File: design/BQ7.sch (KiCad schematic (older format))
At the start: 43 parts

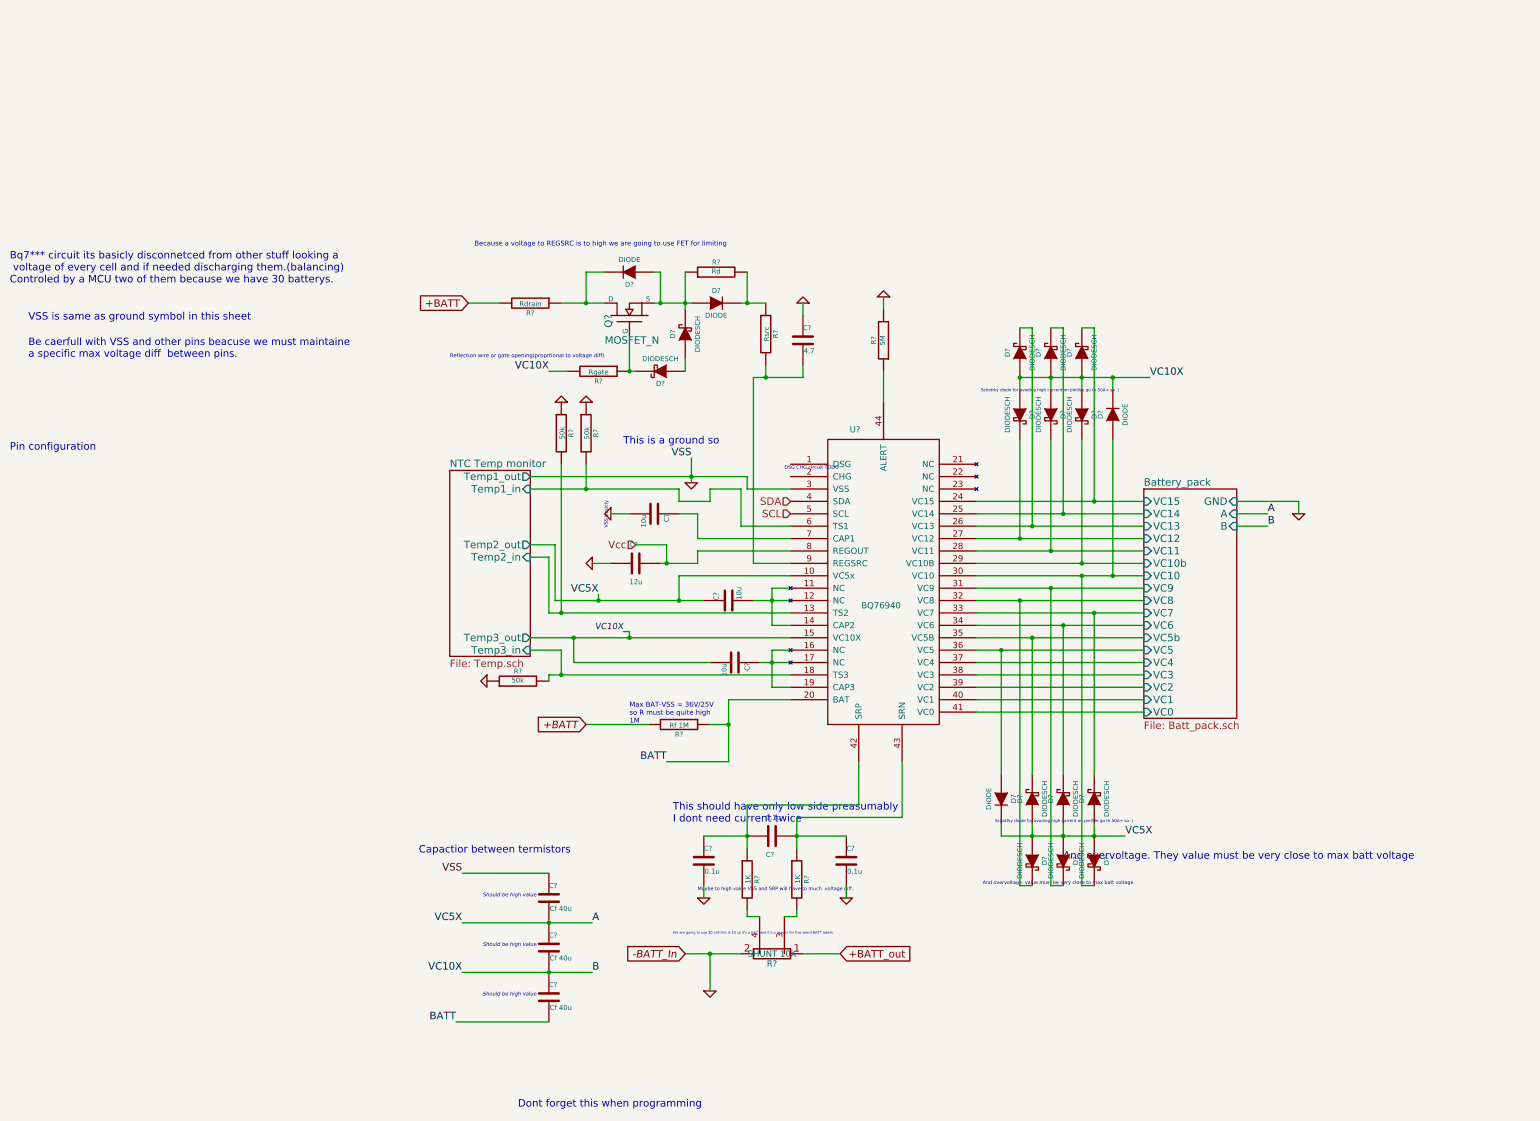
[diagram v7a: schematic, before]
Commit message: Add new example in datasheet define more values
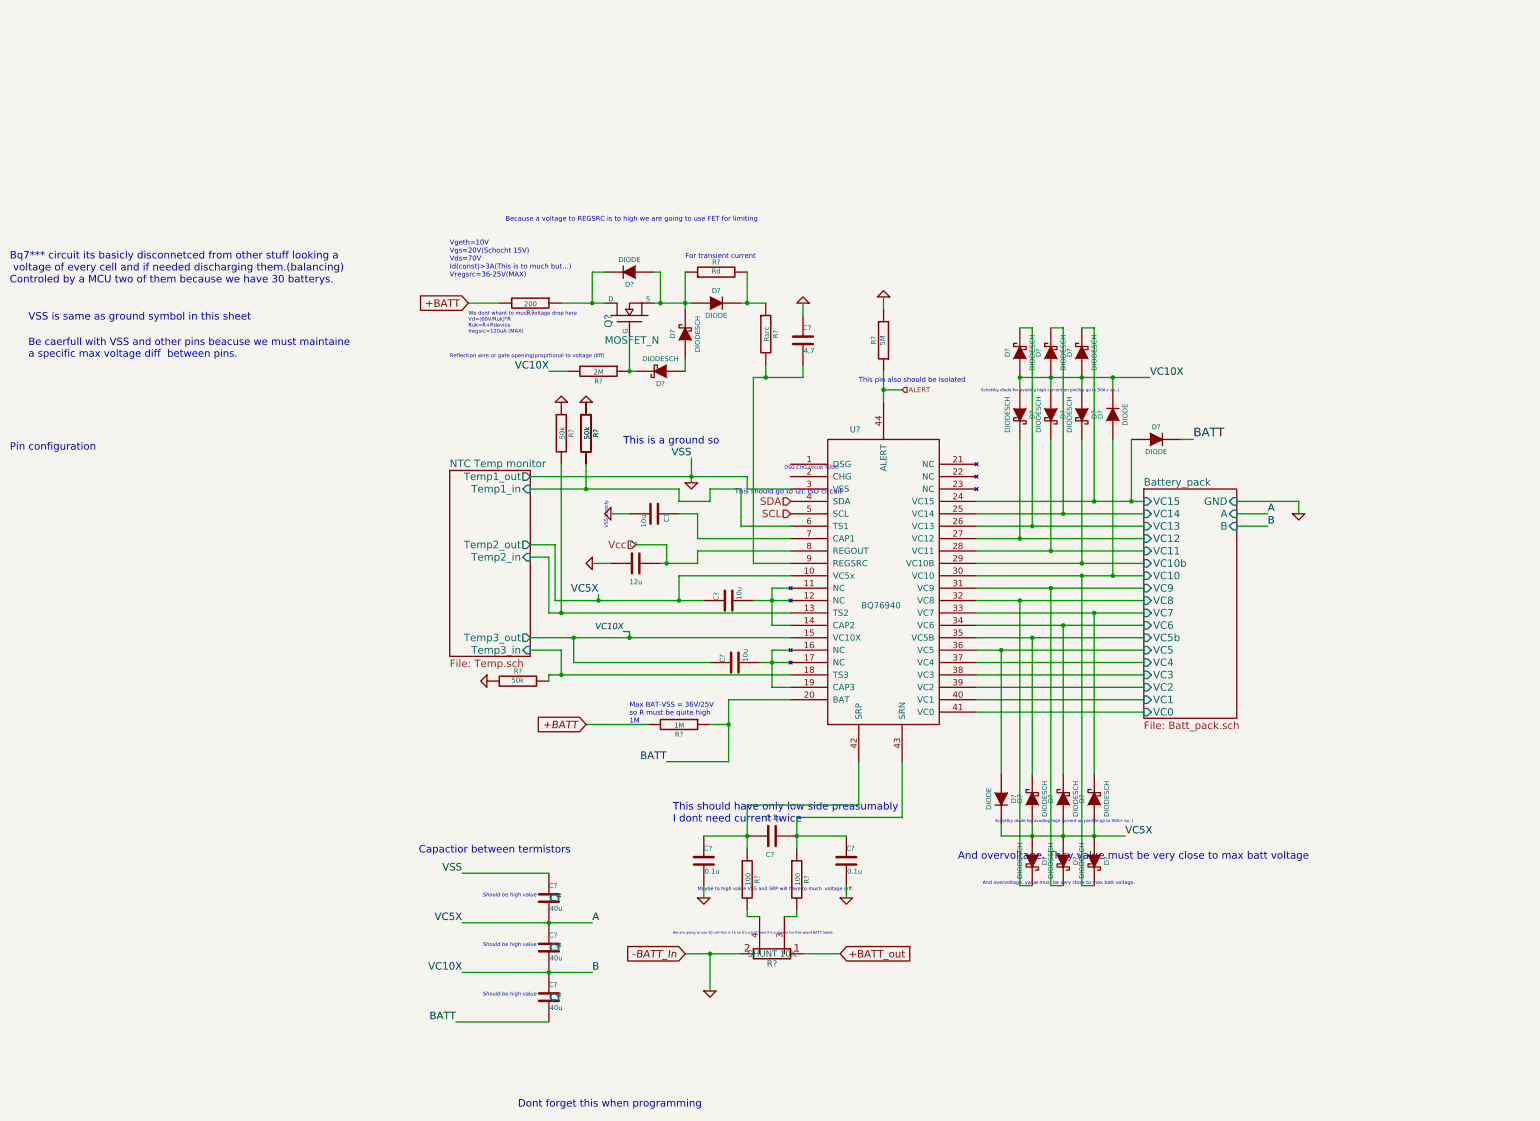
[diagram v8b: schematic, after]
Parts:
- removed C? (x2): Cf 40u, symbol C
- added C? (x2): 40u, symbol C
- added D?: DIODE, symbol DIODE
- added R?: 50k, symbol R
- C?: value Cf 40u -> 40u; Name (none) -> Cf
- R? (x2): value 1K -> 100
- R?: value Rgate -> 2M; Name (none) -> Rgate
- R?: value Rdrain -> 200; Name (none) -> Rdrain
- R?: value Rf 1M -> 1M; Name (none) -> Rf
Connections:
- net A: now also C?.1, C?.2
- net B: now also C?.1, C?.2; no longer C?.2
- net BATT: now also D?.2 (K)
- net Battery_pack/VC15: now also D?.1 (A)
- net GND: now also C?.1, R?.1
- net NTC Temp monitor/Temp1_in: now also R?.2
- net ALERT: now reaches R?.1, U?.44 (ALERT)
- net at U?.16 (NC), U?.17 (NC), U?.19 (CAP3): now also C?.2; no longer C?.1
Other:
- note added: "For transient current"
- note added: "This pin also should be isolated"
- note added: "This should go to i2c ISO circuit"
- note added: "Vgeth=10V\nVgs=20V(Schocht 15V)\nVds=70V\nId(const)>3A(This is to much but...)\nVregsrc=36-25V(MAX)"
- note added: "We dont whant to much voltage drop here\nVd=(60V/Ruk)*R\nRuk=R+Rdevice\nIregsrc=120uA (MAX)\n \n"
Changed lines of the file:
@@
 9F DF D1 D1 31 D6 A5 40 90 E1 4D 94 96 C0 77 F7 E1 9C E9 BB 40 B5 84 6A 00 41 90 F1 06 B5 8D 23
 08 82 20 C8 04 83 62 36 82 20 08 82 4C 0C 38 D4 12 88 20 08 82 20 E3 1C 1A 1D 89 20 08 82 20 08
-82 20 08 82 20 23 ED FF 01 11 4E 07 64 6B 3C CF 2D 00 00 00 00 49 45 4E 44 AE 42 60 82 A6
+82 20 08 82 20 23 ED FF 01 11 4E 07 64 6B 3C CF 2D 00 00 00 00 49 45 4E 44 AE 42 60 82 6A
 EndData
 $EndBitmap
@@
 P 6600 5650
 F 0 "R?" V 6680 5650 40  0000 C CNN
-F 1 "1K" V 6607 5651 40  0000 C CNN
+F 1 "100" V 6607 5651 40  0000 C CNN
 F 2 "" V 6530 5650 30  0000 C CNN
 F 3 "" H 6600 5650 30  0000 C CNN
@@
 P 7000 5650
 F 0 "R?" V 7080 5650 40  0000 C CNN
-F 1 "1K" V 7007 5651 40  0000 C CNN
+F 1 "100" V 7007 5651 40  0000 C CNN
 F 2 "" V 6930 5650 30  0000 C CNN
 F 3 "" H 7000 5650 30  0000 C CNN
@@
 P 6050 4400
 F 0 "R?" V 6130 4400 40  0000 C CNN
-F 1 "Rf 1M" V 6057 4401 40  0000 C CNN
+F 1 "1M" V 6057 4401 40  0000 C CNN
 F 2 "" V 5980 4400 30  0000 C CNN
 F 3 "" H 6050 4400 30  0000 C CNN
+F 4 "Rf" V 6050 4400 60  0001 C CNN "Name"
 	1    6050 4400
 	0    1    1    0
@@
 P 5400 1550
 F 0 "R?" V 5480 1550 40  0000 C CNN
-F 1 "Rgate" V 5407 1551 40  0000 C CNN
+F 1 "2M" V 5407 1551 40  0000 C CNN
 F 2 "" V 5330 1550 30  0000 C CNN
 F 3 "" H 5400 1550 30  0000 C CNN
+F 4 "Rgate" V 5400 1550 60  0001 C CNN "Name"
 	1    5400 1550
 	0    1    1    0
@@
 P 4850 1000
 F 0 "R?" V 4930 1000 40  0000 C CNN
-F 1 "Rdrain" V 4857 1001 40  0000 C CNN
+F 1 "200" V 4857 1001 40  0000 C CNN
 F 2 "" V 4780 1000 30  0000 C CNN
 F 3 "" H 4850 1000 30  0000 C CNN
+F 4 "Rdrain" V 4850 1000 60  0001 C CNN "Name"
 	1    4850 1000
 	0    1    1    0
@@
 Text Label 4300 6000 2    60   ~ 0
 VC5X
-$Comp
-L C C?
-U 1 1 55BD7EDC
-P 5000 5800
-F 0 "C?" H 5000 5900 40  0000 L CNN
-F 1 "Cf 40u" H 5006 5715 40  0000 L CNN
-F 2 "" H 5038 5650 30  0000 C CNN
-F 3 "" H 5000 5800 60  0000 C CNN
-	1    5000 5800
-	1    0    0    -1
-$EndComp
-$Comp
-L C C?
-U 1 1 55BD7FD5
-P 5000 6200
-F 0 "C?" H 5000 6300 40  0000 L CNN
-F 1 "Cf 40u" H 5006 6115 40  0000 L CNN
-F 2 "" H 5038 6050 30  0000 C CNN
-F 3 "" H 5000 6200 60  0000 C CNN
-	1    5000 6200
-	1    0    0    -1
-$EndComp
 Text Label 5950 4700 2    60   ~ 0
 BATT
@@
 P 5000 6600
 F 0 "C?" H 5000 6700 40  0000 L CNN
-F 1 "Cf 40u" H 5006 6515 40  0000 L CNN
+F 1 "40u" H 5006 6515 40  0000 L CNN
 F 2 "" H 5038 6450 30  0000 C CNN
 F 3 "" H 5000 6600 60  0000 C CNN
+F 4 "Cf" H 5001 6600 60  0000 L CNB "Name"
 	1    5000 6600
 	1    0    0    -1
@@
 Text Notes 4900 6600 2    30   Italic 0
 Should be high value\n
-Text Notes 4400 550  0    39   ~ 0
+Text Notes 4650 350  0    39   ~ 0
 Because a voltage to REGSRC is to high we are going to use FET for limiting
 Text Notes 4200 1450 0    31   ~ 0
@@
 Text Notes 6000 6100 0    20   ~ 0
 We are going to use 30 cell this is 15 so it's a half here it's a reason for this wierd BATT labels
-Text Notes 9150 5500 0    60   ~ 0
+Text Notes 8300 5500 0    60   ~ 0
 And overvoltage. They value must be very close to max batt voltage
 Text Notes 8500 5700 0    28   ~ 0
@@
 F 3 "" H 6500 3900 60  0000 C CNN
 	1    6500 3900
-	0    1    1    0
+	0    -1   -1   0
 $EndComp
 $Comp
@@
 Text Notes 6000 5200 0    60   ~ 0
 This should have only low side preasumably\nI dont need current twice
+Text Notes 6500 2550 0    40   ~ 0
+This should go to i2c ISO circuit
+$Comp
+L R R?
+U 1 1 55DBFB03
+P 5300 2050
+F 0 "R?" V 5380 2050 40  0000 C CNN
+F 1 "50k" V 5307 2051 40  0000 C CNN
+F 2 "" V 5230 2050 30  0000 C CNN
+F 3 "" H 5300 2050 30  0000 C CNN
+	1    5300 2050
+	1    0    0    -1
+$EndComp
+$Comp
+L C C?
+U 1 1 55DC3CEE
+P 5000 6200
+F 0 "C?" H 5000 6300 40  0000 L CNN
+F 1 "40u" H 5006 6115 40  0000 L CNN
+F 2 "" H 5038 6050 30  0000 C CNN
+F 3 "" H 5000 6200 60  0000 C CNN
+F 4 "Cf" H 5001 6200 60  0000 L CNB "Name"
+	1    5000 6200
+	1    0    0    -1
+$EndComp
+$Comp
+L C C?
+U 1 1 55DC3FA9
+P 5000 5800
+F 0 "C?" H 5000 5900 40  0000 L CNN
+F 1 "40u" H 5006 5715 40  0000 L CNN
+F 2 "" H 5038 5650 30  0000 C CNN
+F 3 "" H 5000 5800 60  0000 C CNN
+F 4 "Cf" H 5001 5800 60  0000 L CNB "Name"
+	1    5000 5800
+	1    0    0    -1
+$EndComp
+Text HLabel 7850 1700 2    40   Input ~ 0
+ALERT
+Text Notes 7500 1650 0    40   ~ 0
+This pin also should be isolated
+Text Label 10200 2100 0    70   ~ 0
+BATT
+$Comp
+L DIODE D?
+U 1 1 55DE2295
+P 9900 2100
+F 0 "D?" H 9900 2200 40  0000 C CNN
+F 1 "DIODE" H 9900 2000 40  0000 C CNN
+F 2 "" H 9900 2100 60  0000 C CNN
+F 3 "" H 9900 2100 60  0000 C CNN
+	1    9900 2100
+	1    0    0    -1
+$EndComp
+Text Notes 4200 800  0    40   ~ 0
+Vgeth=10V\nVgs=20V(Schocht 15V)\nVds=70V\nId(const)>3A(This is to much but...)\nVregsrc=36-25V(MAX)
 Wire Wire Line
 	7700 1050 7700 950
@@
 	5100 1000 5450 1000
 Wire Wire Line
-	5300 1000 5300 750
-Connection ~ 5300 1000
-Wire Wire Line
 	5700 1550 5650 1550
 Connection ~ 5650 1550
@@
 	5900 750  5850 750
 Connection ~ 5900 1000
-Wire Wire Line
-	5300 750  5450 750
 Connection ~ 6100 1000
 Wire Wire Line
@@
 Connection ~ 9400 2600
 Wire Wire Line
-	7700 1800 7700 1550
+	7700 1550 7700 1800
 Wire Wire Line
 	7050 1000 7050 1100
@@
 	5500 2700 5650 2700
 Wire Wire Line
-	6150 2450 6150 2250
+	6150 2250 6150 2450
 Wire Wire Line
 	5100 4000 5100 3800
@@
 	6800 3300 6800 3600
 Wire Wire Line
-	6950 3500 5000 3500
+	5000 3500 6950 3500
 Wire Wire Line
 	5000 3500 5000 3050
@@
 	5000 3050 4850 3050
 Wire Wire Line
-	6250 3400 5050 3400
+	5050 3400 6250 3400
 Wire Wire Line
 	5050 3400 5050 2950
@@
 	6600 2500 6950 2500
 Wire Wire Line
-	6600 2500 6600 2400
-Wire Wire Line
-	6600 2400 4850 2400
+	6600 2400 6600 2500
+Wire Wire Line
+	4850 2400 6600 2400
 Wire Wire Line
 	6950 2800 6550 2800
@@
 	5000 4050 5000 4000
 Connection ~ 5100 4000
+Wire Wire Line
+	7700 1700 7850 1700
+Connection ~ 7700 1700
+Wire Wire Line
+	10100 2100 10200 2100
+Wire Wire Line
+	9700 2100 9700 2600
+Connection ~ 9700 2600
+Wire Wire Line
+	5450 750  5350 750
+Wire Wire Line
+	5350 750  5350 1000
+Connection ~ 5350 1000
+Text Notes 4350 1300 0    30   ~ 0
+We dont whant to much voltage drop here\nVd=(60V/Ruk)*R\nRuk=R+Rdevice\nIregsrc=120uA (MAX)\n		\n
+Text Notes 6100 650  0    40   ~ 0
+For transient current
 $EndSCHEMATC
